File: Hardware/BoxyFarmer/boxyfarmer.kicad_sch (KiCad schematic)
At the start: 7 parts

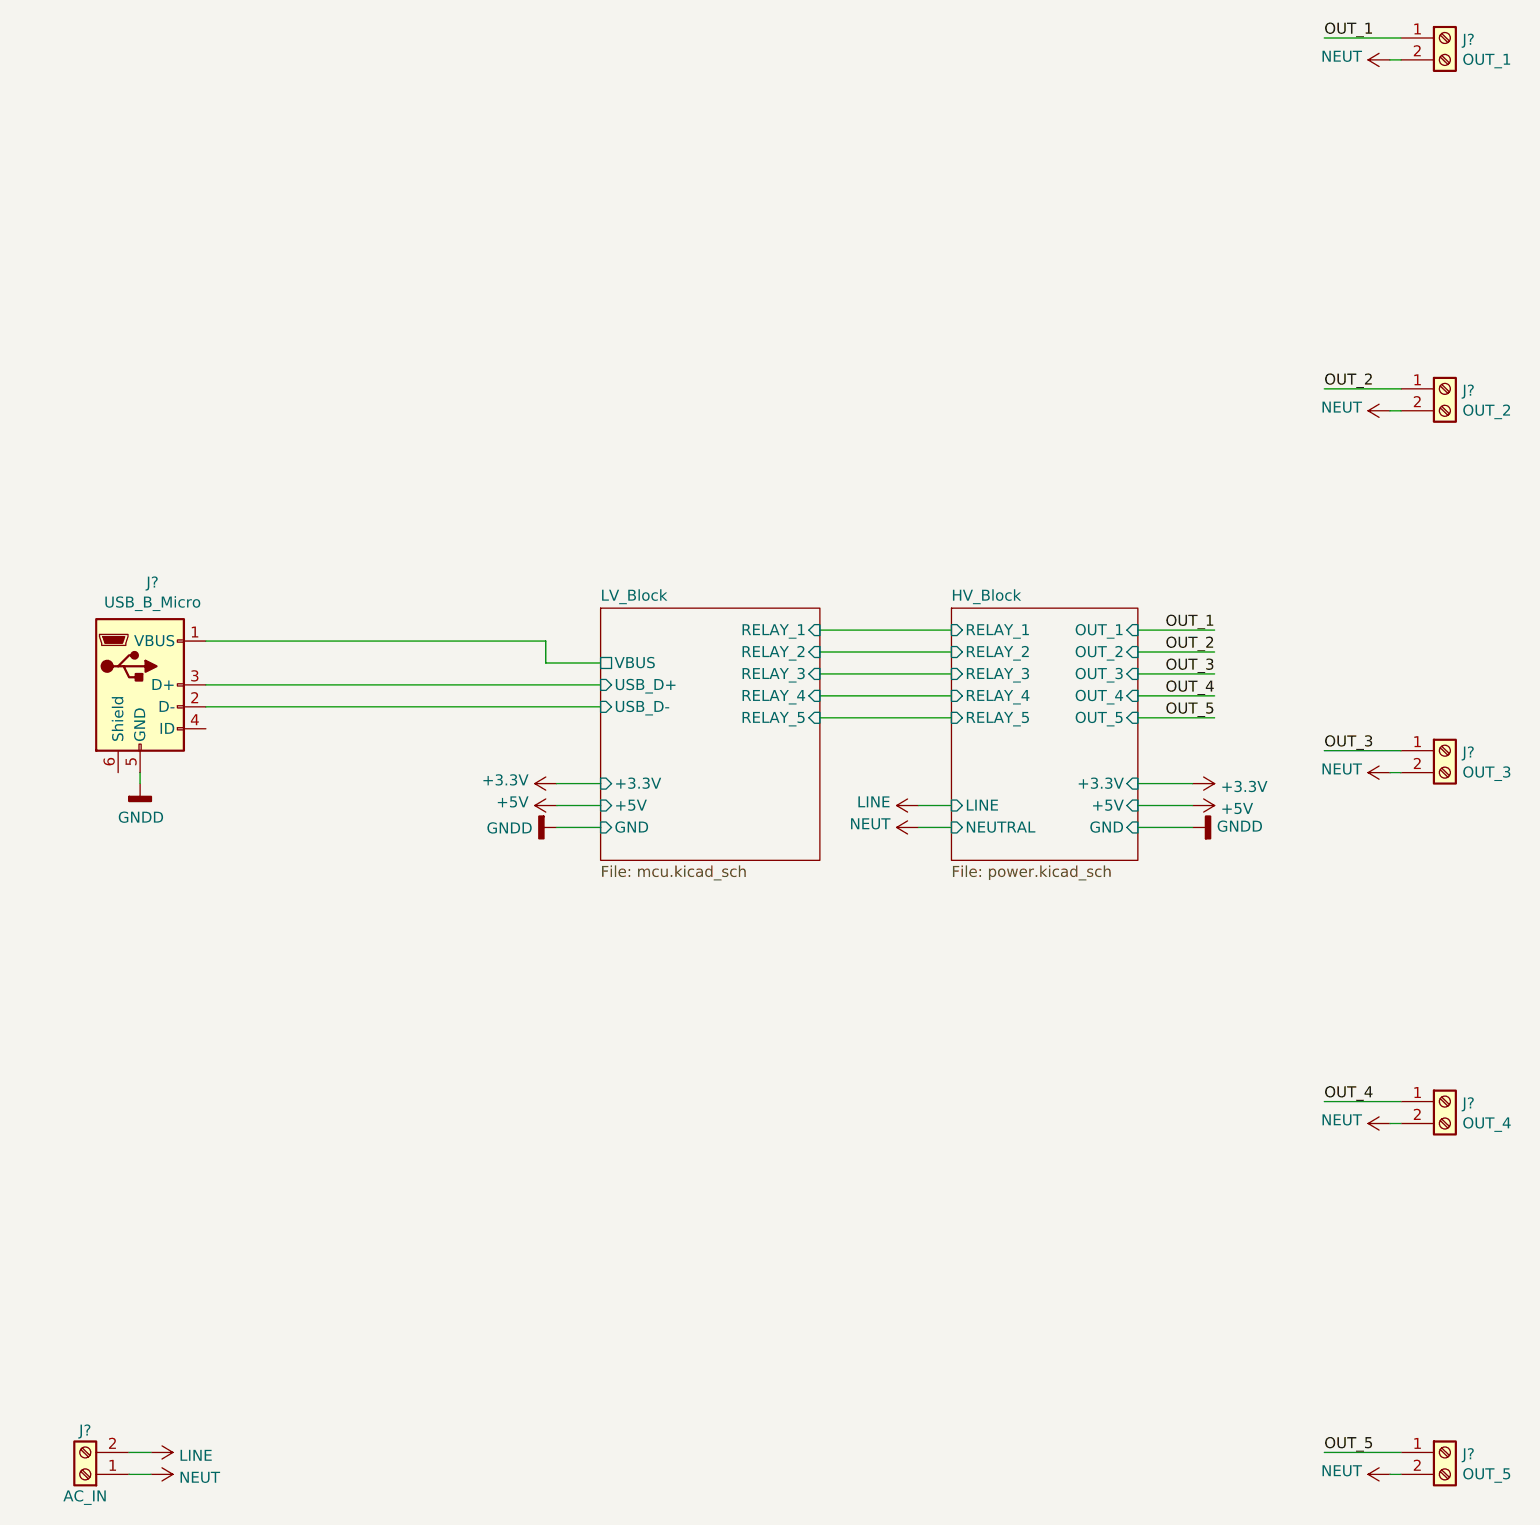
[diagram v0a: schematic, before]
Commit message: Changed Schematic structure, USB connector type changed from MicroUSB to MiniUSB
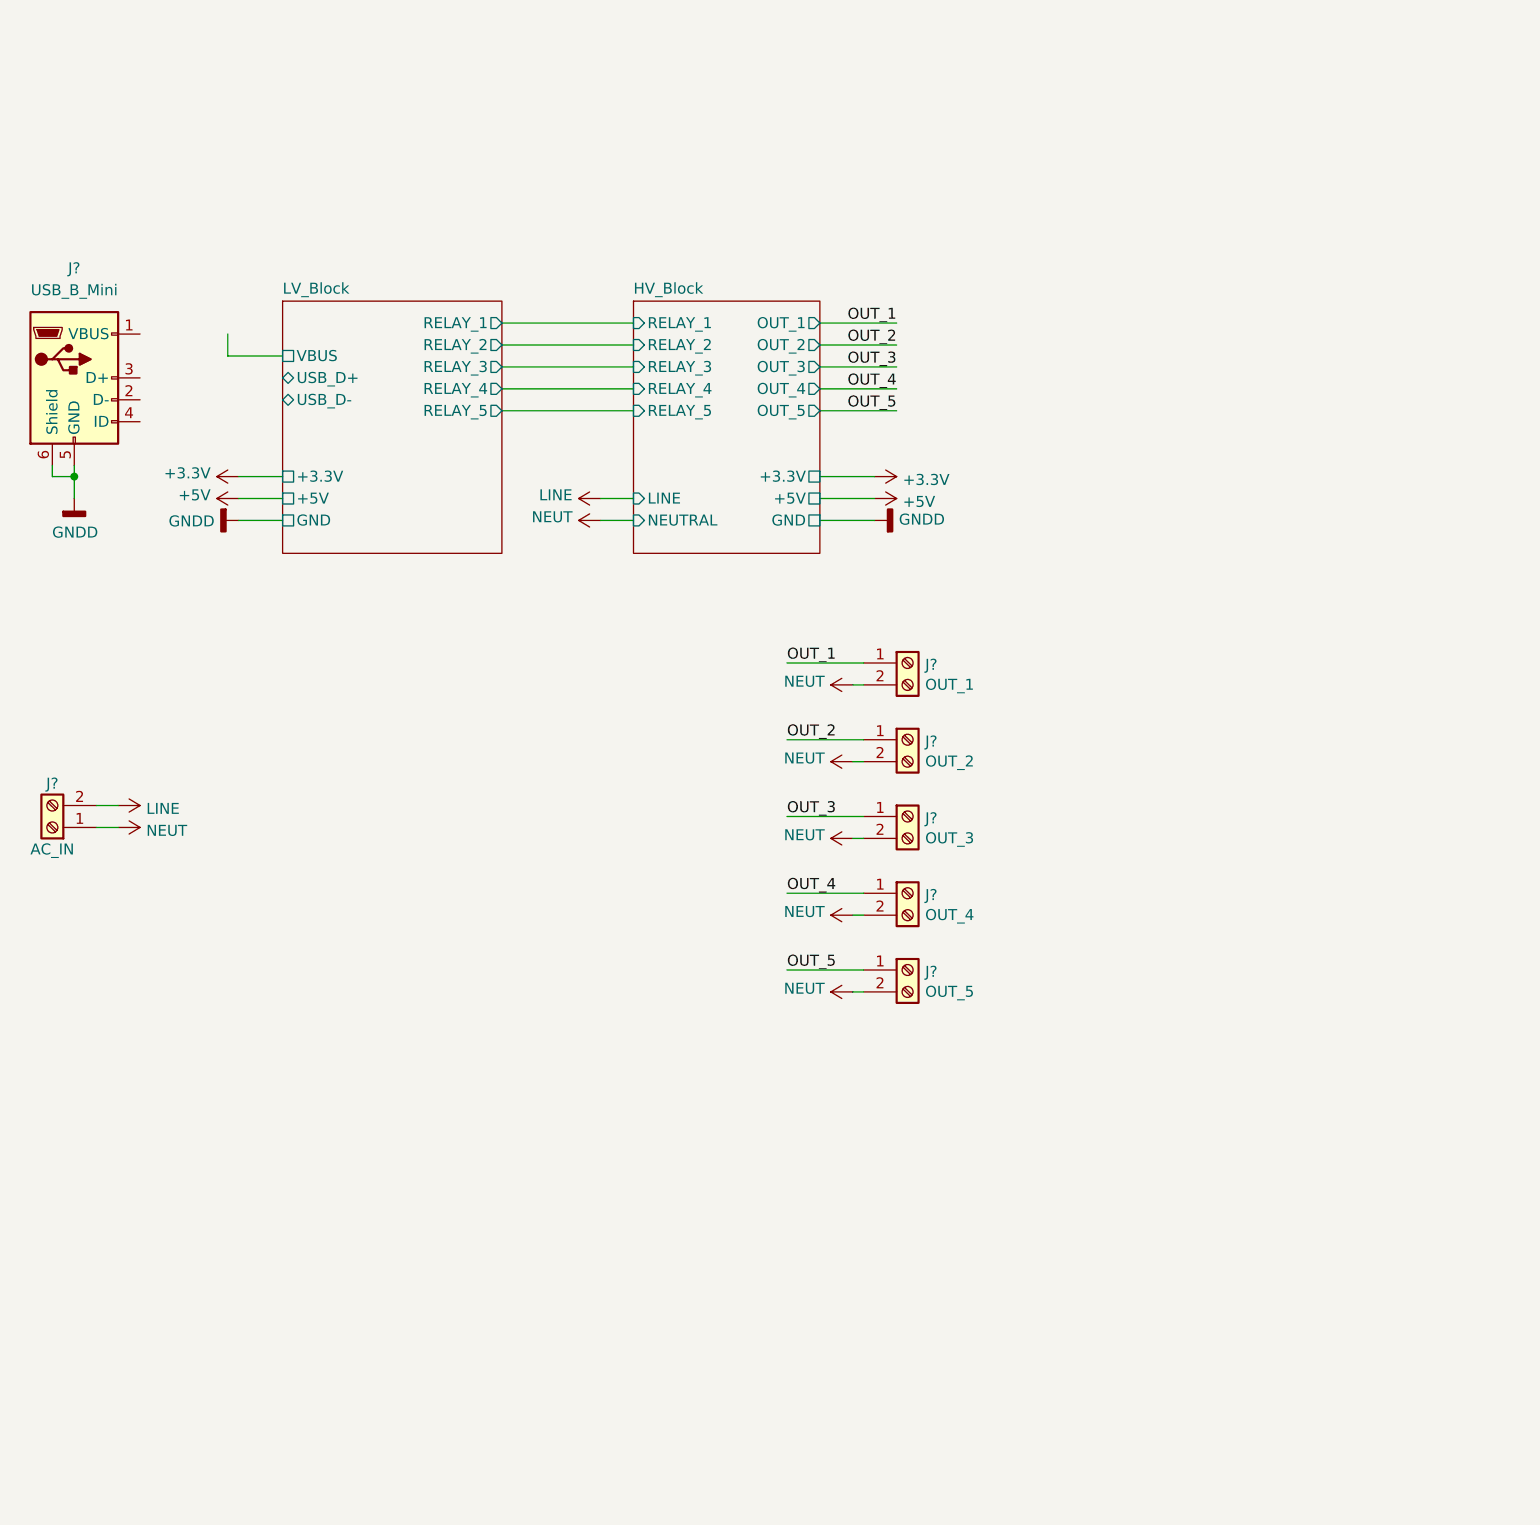
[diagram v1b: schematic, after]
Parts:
- removed J?: USB_B_Micro, symbol Connector:USB_B_Micro
- added J?: USB_B_Mini, symbol Connector:USB_B_Mini
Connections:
- net GNDD: now also J?.5 (GND), J?.6 (Shield)
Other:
- sheet HV_Block: file power.kicad_sch -> high_voltage_block.kicad_sch
- sheet LV_Block: file mcu.kicad_sch -> low_voltage_block.kicad_sch
- title: (none) -> BoxyFarmer
- moved on the sheet: J?
